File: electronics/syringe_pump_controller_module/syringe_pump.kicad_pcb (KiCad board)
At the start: 2 copper layers, 65 x 100 mm, 119 parts, among them J1 IN, J10 EndSwitch, J11 EndSwitch, J12 Conn_01x04, J13 Conn_01x08, J2 ON OFF, J4 HDR-4x1, J5 HDR-4x1, J6 EndSwitch, J7 EndSwitch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

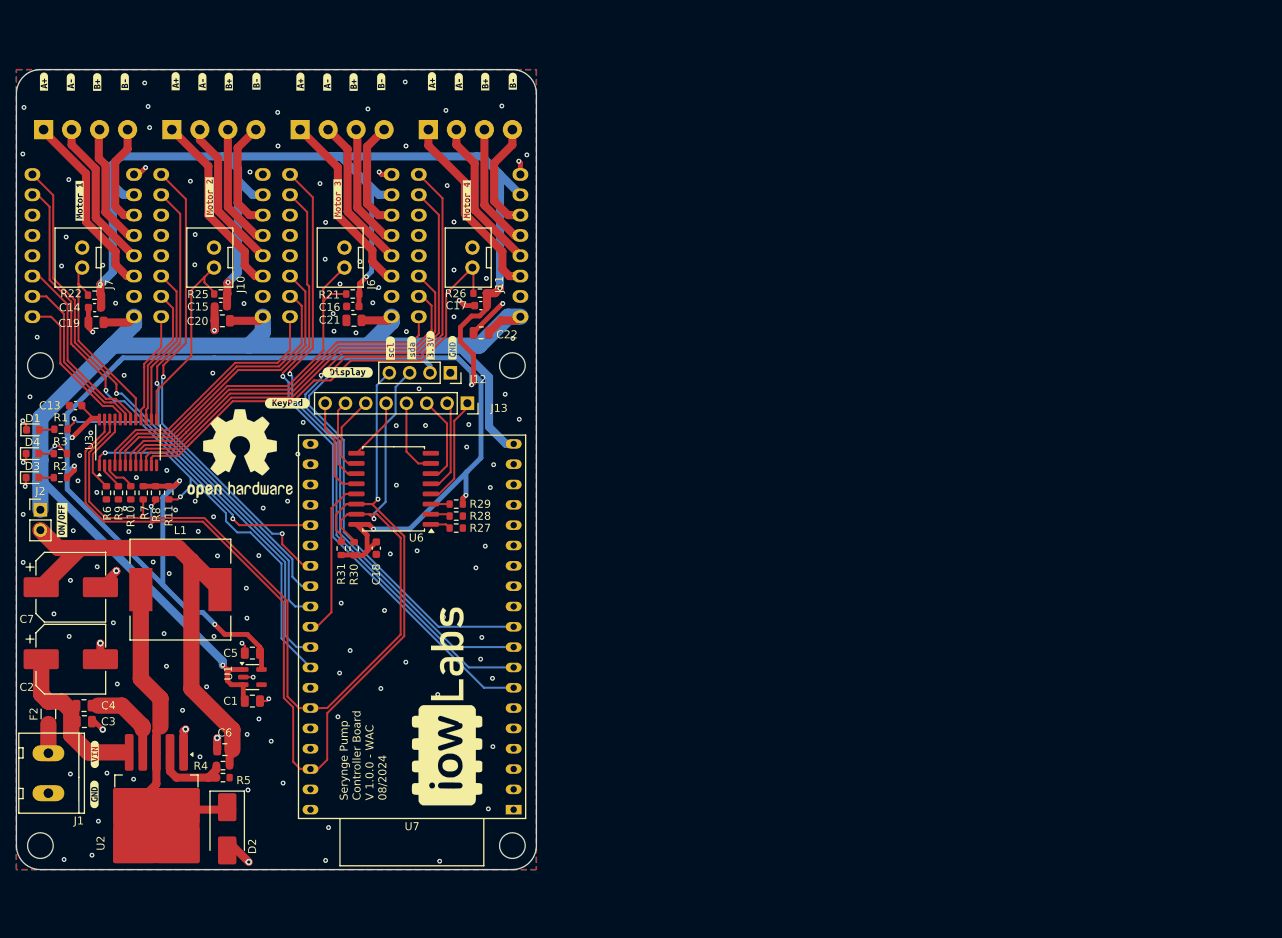
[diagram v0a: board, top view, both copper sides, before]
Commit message: v2 of module version. fixing minor bugs and redistribute components on the board
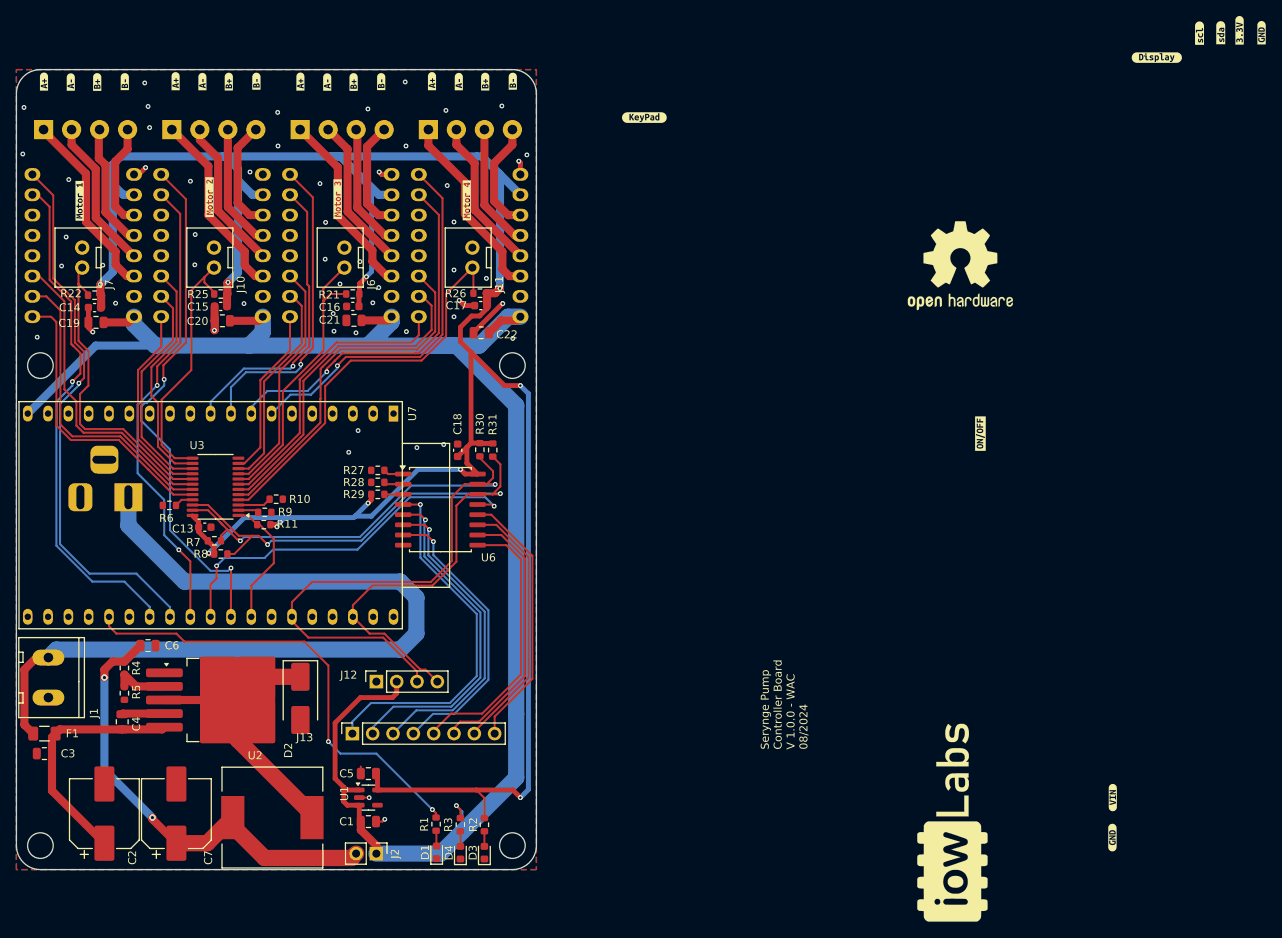
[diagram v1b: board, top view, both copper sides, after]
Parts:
- removed F2: FUSE, Fuse:Fuse_1206_3216Metric
- added F1: FUSE, Fuse:Fuse_1206_3216Metric, F.Cu at (53.5, 133.0)
- added J3: HDR-3x1, Connector_BarrelJack:BarrelJack_Horizontal, B.Cu at (64.0, 103.5)
- J1: value IN -> VIN
- moved kibuzzard-66A40617 127.4 mm to (187.1, 141.0)
- moved kibuzzard-66A405FA 127.4 mm to (187.0, 146.0)
- moved G*** 125.4 mm to (191.0, 89.0)
- moved kibuzzard-66C26F7C 115.3 mm to (170.5, 95.5)
- moved kibuzzard-66C27154 108.5 mm to (192.6, 48.5)
- moved kibuzzard-66C271FC 108.5 mm to (200.5, 45.4)
- moved kibuzzard-66C27168 108.5 mm to (205.6, 45.4)
- moved kibuzzard-66C27204 108.5 mm to (197.9, 45.4)
- moved kibuzzard-66C27224 108.5 mm to (202.9, 45.1)
- moved G*** 108.4 mm to (179.5, 146.5), turned to -90 degrees
- moved REF** 93.1 mm to (168.0, 74.5)
- moved D3 73.4 mm to (108.5, 147.9), turned to 90 degrees
- moved D4 73.2 mm to (105.5, 147.9), turned to 90 degrees
- moved D1 73.1 mm to (102.5, 147.8), turned to 90 degrees
- moved R2 68.5 mm to (108.5, 144.4), turned to -90 degrees
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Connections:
- J1 pad 2: Net-(F2-Pad1) -> /VIN
- J12 pad 2: +3V3 -> VM
- U3 pad 10: M4_MS2 -> M3_MS1
- U3 pad 11: M4_ES -> M3_EN
- U3 pad 22: SDA -> SCL
- U3 pad 23: SCL -> SDA
- U3 pad 4: M3_EN -> M4_ES
- U3 pad 5: M3_MS1 -> M4_MS2
- U3 pad 6: M3_MS2 -> M4_MS1
- U3 pad 7: M3_ES -> M4_EN
- U3 pad 8: M4_EN -> M3_ES
- U3 pad 9: M4_MS1 -> M3_MS2
- U7 pad 10: M4_DIR -> M3_STEP
- U7 pad 26: M2_DIR -> M1_STEP
- U7 pad 27: M2_STEP -> M1_DIR
- U7 pad 28: M1_DIR -> M2_STEP
- U7 pad 30: M1_STEP -> M2_DIR
- U7 pad 7: M3_STEP -> M4_DIR
- U7 pad 8: M3_DIR -> M4_STEP
- U7 pad 9: M4_STEP -> M3_DIR
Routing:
- net /VIN: track 0.00 -> 107.1 mm
- net VM: track 174.5 -> 216.6 mm, vias 2 -> 1
- net M3_STEP: track 78.1 -> 36.9 mm
- net SCL: track 137.0 -> 96.5 mm, vias 3 -> 2
- net M3_DIR: track 78.9 -> 39.0 mm
- net M4_DIR: track 86.2 -> 46.9 mm
- net M4_STEP: track 85.3 -> 46.7 mm
- net INT_MGA: track 49.4 -> 16.6 mm, vias 2 -> 0
- net Net-(J13-Pin_1): track 13.8 -> 45.9 mm, vias 0 -> 1
- net +3V3: track 338.4 -> 307.4 mm, vias 11 -> 10
- net Net-(J13-Pin_2): track 11.9 -> 42.5 mm, vias 0 -> 1
- net Net-(J13-Pin_3): track 11.3 -> 39.4 mm, vias 0 -> 1
- net INT_KP: track 20.2 -> 47.6 mm, vias 0 -> 2
- net Net-(J13-Pin_5): track 7.79 -> 34.7 mm
- net Net-(J13-Pin_4): track 9.71 -> 36.4 mm, vias 0 -> 1
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
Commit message: adding gerber files for V2
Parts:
- removed the G*** at (191.0, 89.0)
- removed kibuzzard-66C27224: G***, kibuzzard-66C27224
- added G***: LOGO, IoWLabsLogos:LIBRE_HUB, B.Cu at (75.5, 140.4)
- added G***: LOGO, IoWLabsLogos:wenzel_lab_small, B.Cu at (82.4, 105.1)
- added kibuzzard-678D3724: G***, kibuzzard-678D3724, F.Cu at (99.5, 144.5)
- added kibuzzard-678D3737: G***, kibuzzard-678D3737, F.Cu at (102.6, 144.5)
- added kibuzzard-678D375F: G***, kibuzzard-678D375F, F.Cu at (105.6, 144.6)
- added kibuzzard-678D37F1: G***, kibuzzard-678D37F1, F.Cu at (97.5, 123.7)
- G*** (x2): moved to F.Cu
- G***: moved to B.Cu
- moved kibuzzard-66C27168 135.3 mm to (95.0, 123.3)
- moved kibuzzard-66A405FA 128.7 mm to (59.4, 128.8)
- moved kibuzzard-66A40617 128.7 mm to (59.5, 123.8)
- moved kibuzzard-66C271FC 127.1 mm to (100.2, 123.5)
- moved kibuzzard-66C27204 123.0 mm to (102.8, 123.5)
- moved kibuzzard-66C27154 121.1 mm to (102.2, 129.1)
- moved G*** 98.1 mm to (87.1, 113.5), turned to 0 degrees
- moved G*** 95.5 mm to (73.1, 126.8), turned to 180 degrees
- moved kibuzzard-66C26F7C 91.8 mm to (93.6, 145.7), turned to 0 degrees
- moved kibuzzard-66C27242 82.2 mm to (107.7, 135.5)
- moved G*** 78.5 mm to (81.4, 87.2), turned to 0 degrees
- moved REF** 74.4 mm to (106.3, 116.1)
- moved REF** 58.0 mm to (105.1, 105.4), turned to 180 degrees
- moved D1 1.53 mm to (101.0, 147.8)
- moved D3 1.50 mm to (107.0, 147.9)
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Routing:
- net +3V3: track 307.4 -> 313.6 mm, vias 10 -> 11
- net GND: track 22.3 -> 27.0 mm, vias 54 -> 132
- net Net-(J13-Pin_6): track 34.1 -> 30.5 mm
- net Net-(J13-Pin_5): track 34.7 -> 31.9 mm
- net Net-(J13-Pin_7): track 32.9 -> 30.8 mm
- net LED: track 57.8 -> 59.9 mm
- net Net-(J13-Pin_8): track 33.2 -> 31.3 mm
- net Net-(U3-A1): track 2.59 -> 3.53 mm
- net M4_DIR: track 46.9 -> 47.7 mm
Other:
- board text added: "Serynge Pump Controller Board V 2.0.0 - WAC 01/2025"
- board text removed: "Serynge Pump Controller Board V 1.0.0 - WAC 08/2024"
